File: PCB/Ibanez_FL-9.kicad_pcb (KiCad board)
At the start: 2 copper layers, 60 x 77 mm, 147 parts, among them IC101 TL022, IC102 TL022, IC103 TL022, IC104 MN3207, IC105 MN3102, IC106 LM78L05_TO92, J3 EXT_DC, Q101 2SC2458GR, Q102 2SC2458GR, Q103 2SK44SPC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

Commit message: update original pcb date
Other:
- board text added: "IBANEZ FL9 FLANGER 1982"
- board text removed: "IBANEZ FL9 FLANGER 1985"
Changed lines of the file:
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@@
     (effects (font (size 0.5 0.5) (thickness 0.1)) (justify right mirror))
   )
-  (gr_text "IBANEZ FL9 FLANGER 1985" (at 205 116.5) (layer "B.SilkS")
+  (gr_text "IBANEZ FL9 FLANGER 1982" (at 205 116.5) (layer "B.SilkS")
     (effects (font (size 0.7 0.7) (thickness 0.14)) (justify mirror))
   )
@@
     (effects (font (size 0.5 0.5) (thickness 0.1)) (justify right))
   )
-  (gr_text "IBANEZ FL9 FLANGER 1985" (at 239 55 90) (layer "F.SilkS")
+  (gr_text "IBANEZ FL9 FLANGER 1982" (at 239 55 90) (layer "F.SilkS")
     (effects (font (size 0.7 0.7) (thickness 0.14)))
   )

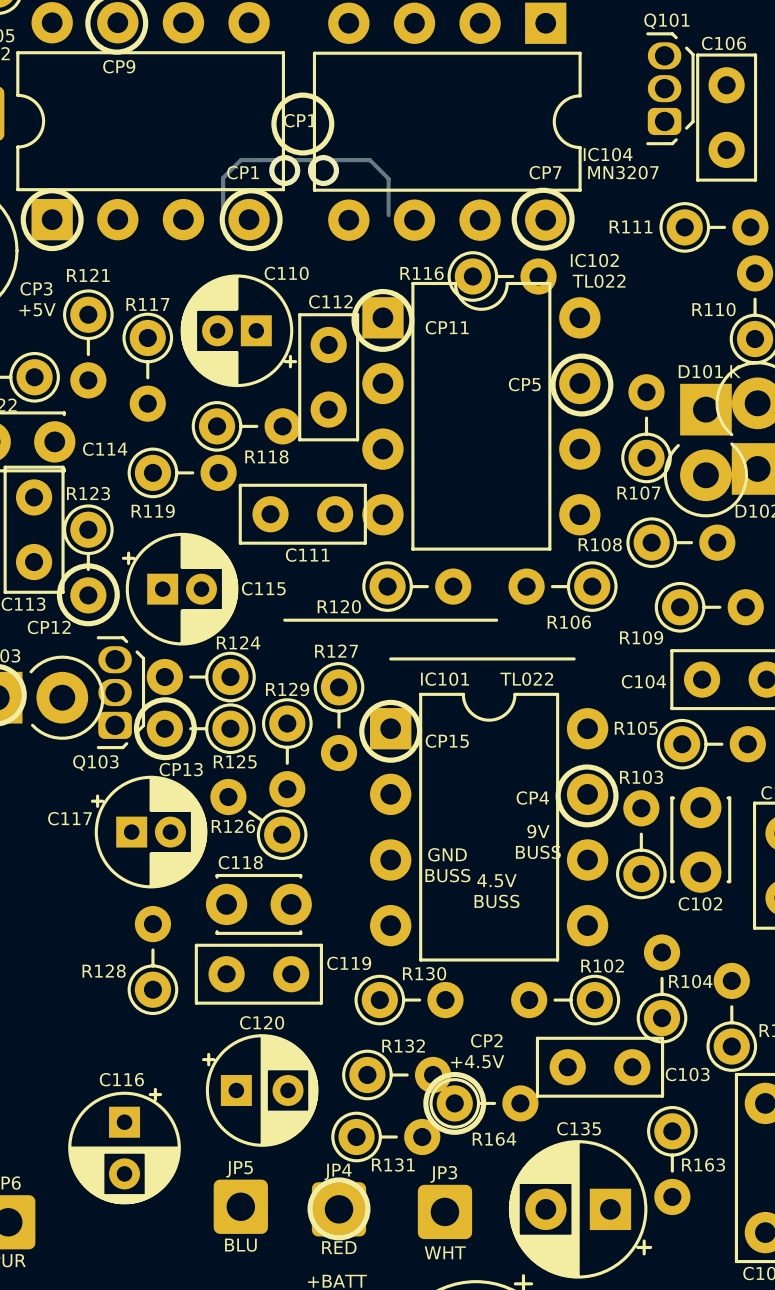
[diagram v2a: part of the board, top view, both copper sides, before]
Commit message: update testpoints on bot silk; fix spelling
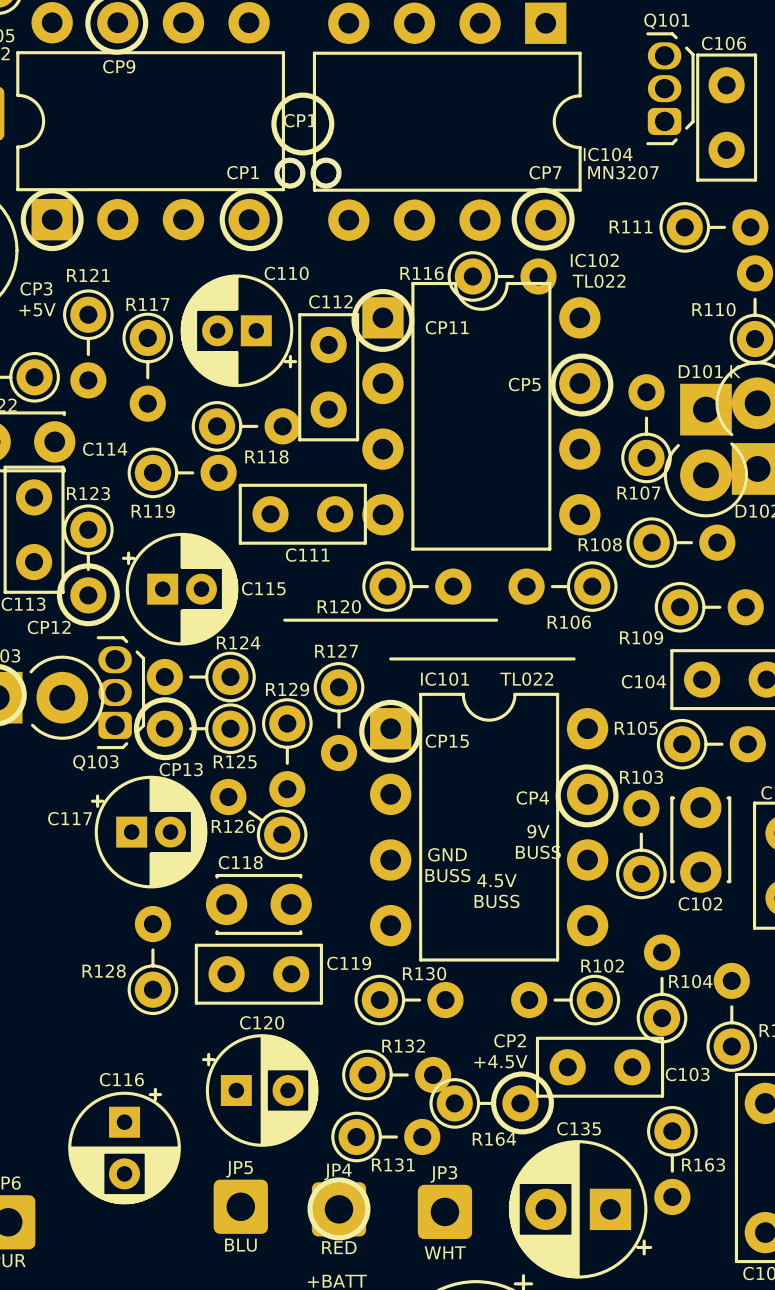
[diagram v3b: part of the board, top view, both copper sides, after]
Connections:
- IC101 pad 4: (no net) -> GND
- IC101 pad 8: (no net) -> +9V
- IC102 pad 4: (no net) -> GND
- IC102 pad 8: (no net) -> +9V
- IC103 pad 4: (no net) -> GND
- IC103 pad 8: (no net) -> +5V
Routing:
- net /CP1: track 9.80 -> 0.00 mm
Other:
- board text added: "CP1 BBD CLOCK"
- board text added: "CP11 LOW-PASS -24dB/OCT"
- board text added: "CP12 LOW-PASS -24dB/OCT OUT"
- board text added: "CP13 BYPASS OUT"
- board text added: "CP14 BYPASS DRIVER"
- board text added: "CP15 MIX/DE-EMPH"
- board text added: "CP4 PRE-EMPH"
- board text added: "CP5 MIX/CLAMP"
- board text added: "CP6 LOW-PASS -12dB/OCT"
- board text added: "CP7 BBD OUT"
- board text added: "CP8 SWEEP+BIAS"
- board text added: "CP9 CLOCK OSC"

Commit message: update jumper and CP1
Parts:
- added G***: LOGO, CedarGrove_custom:CedarGroveStudios_TEXT_LOGO_8x5_4mm, F.Cu at (217.2, 114.3)
- added G***: LOGO, CedarGrove_custom:CedarGroveStudios_TEXT_LOGO_8x5_4mm, B.Cu at (217.4, 114.3)
- added REF**: Pin_D0.7mm_L6.5mm_W1.8mm_FlatFork, Connector_Pin:Pin_D0.7mm_L6.5mm_W1.8mm_FlatFork, F.Cu at (225.4, 77.3)
- added REF**: Pin_D0.7mm_L6.5mm_W1.8mm_FlatFork, Connector_Pin:Pin_D0.7mm_L6.5mm_W1.8mm_FlatFork, F.Cu at (221.2, 78.8)
- added REF**: Pin_D0.7mm_L6.5mm_W1.8mm_FlatFork, Connector_Pin:Pin_D0.7mm_L6.5mm_W1.8mm_FlatFork, F.Cu at (217.7, 59.8)
- added REF**: Pin_D0.7mm_L6.5mm_W1.8mm_FlatFork, Connector_Pin:Pin_D0.7mm_L6.5mm_W1.8mm_FlatFork, F.Cu at (217.1, 77.3)
- added REF**: Pin_D0.7mm_L6.5mm_W1.8mm_FlatFork, Connector_Pin:Pin_D0.7mm_L6.5mm_W1.8mm_FlatFork, F.Cu at (228.5, 78.8)
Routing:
- net /CP1: vias 2 -> 0
